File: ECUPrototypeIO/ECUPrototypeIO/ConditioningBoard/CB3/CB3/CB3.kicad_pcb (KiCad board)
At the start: 2 copper layers, 28 parts, among them J1 ECU Connector 1, J2 ECU Connector 2, J3 Relay Module Con2, J4 Vehicle Connector 1, J5 Relay Module Con1, Q1 MOSFET_A, SW1 MomentarySwitch, SW2 MomentarySwitch, T1 Screw_Terminal_01x04, U1 LM324

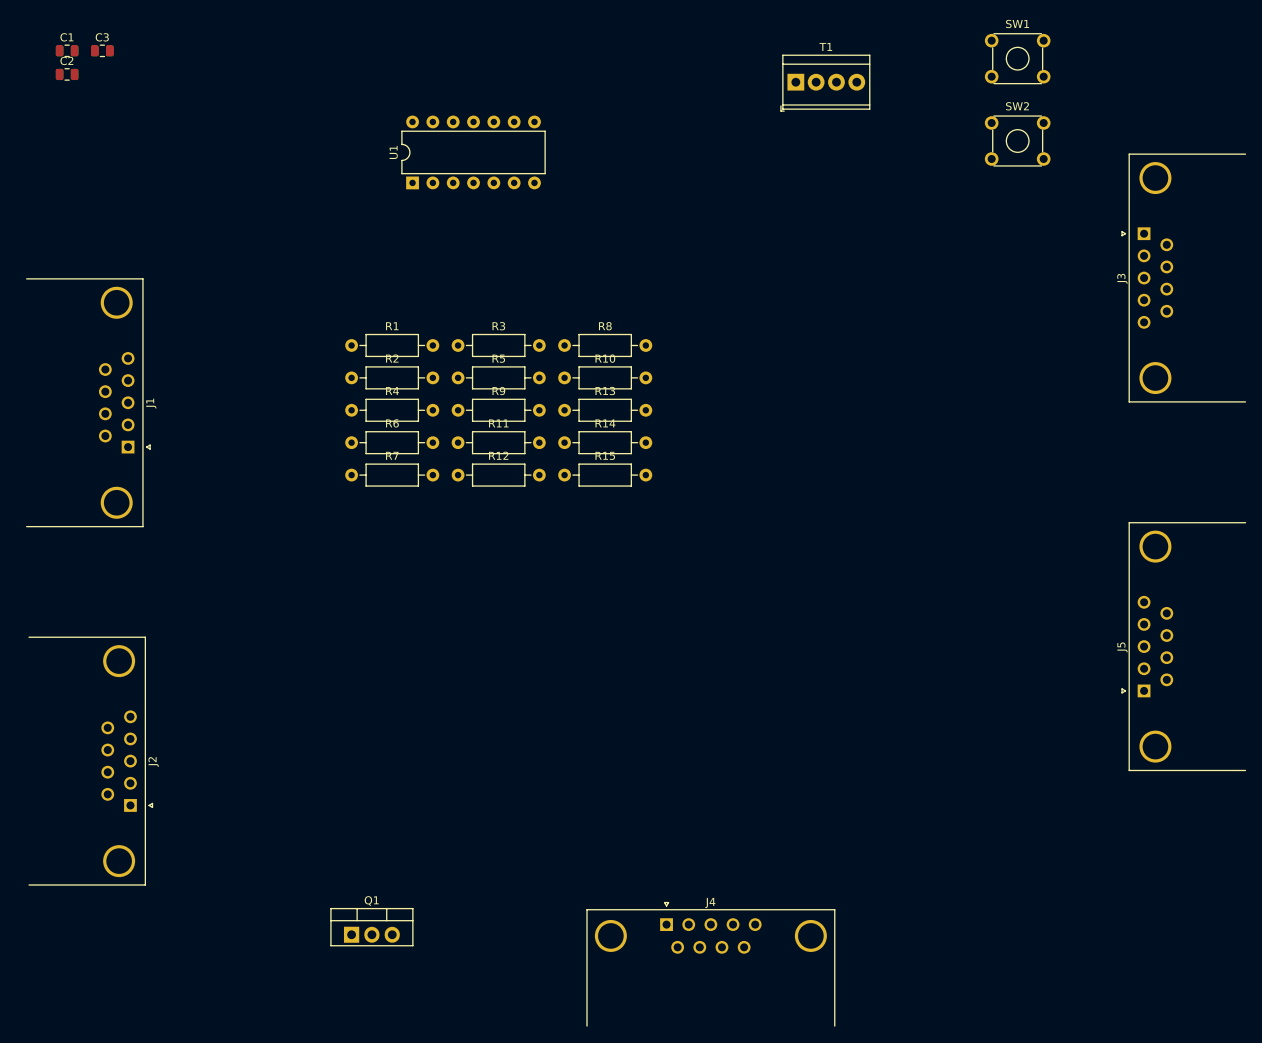
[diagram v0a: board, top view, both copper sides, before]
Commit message: grouped relevant components on PCB Schematic
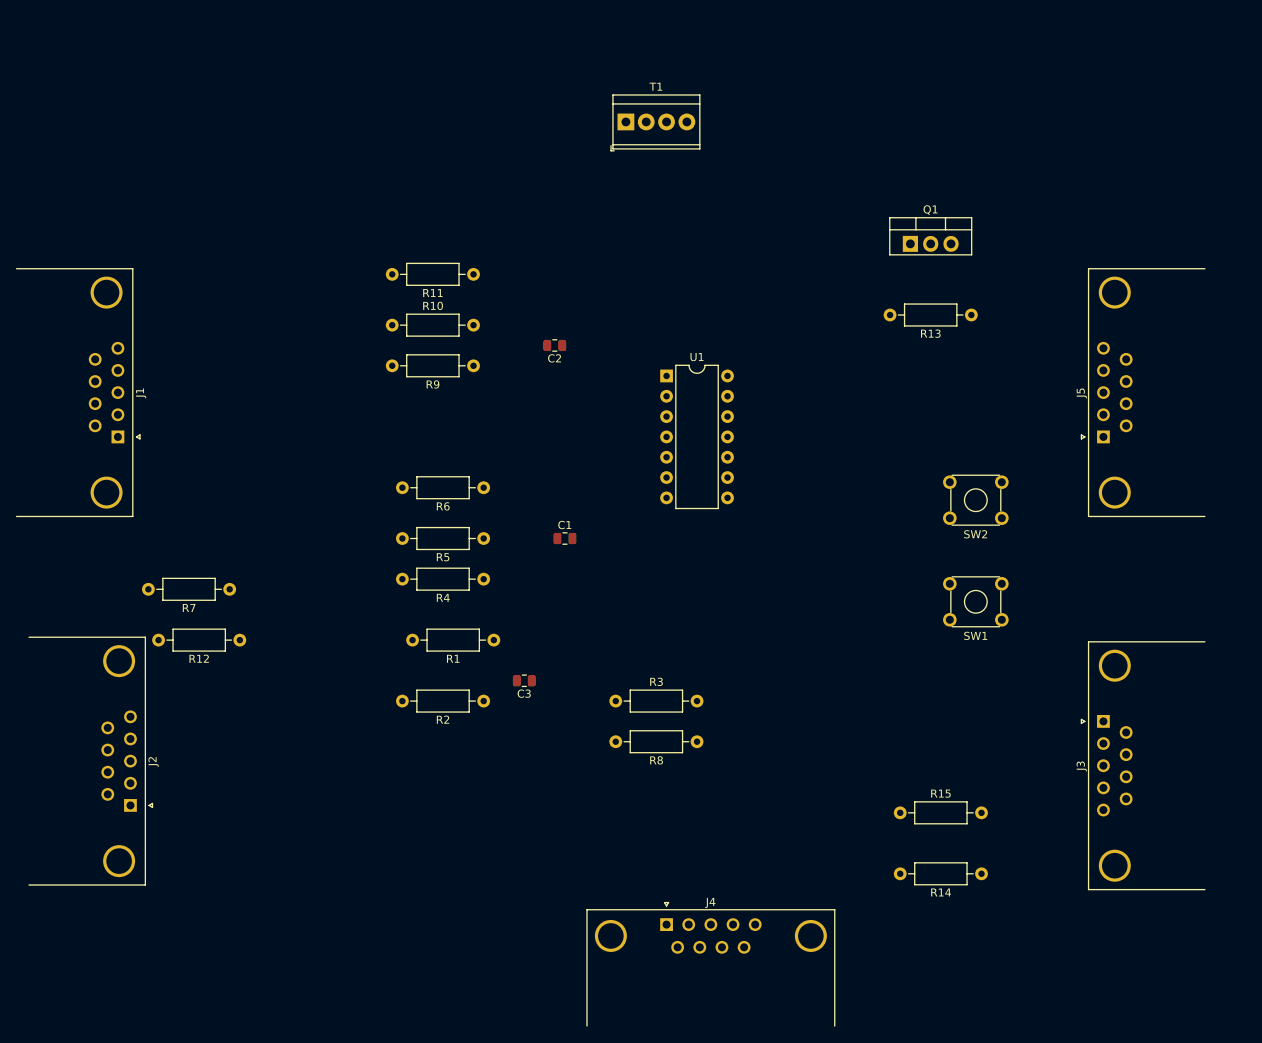
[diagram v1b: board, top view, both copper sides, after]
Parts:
- moved Q1 111.1 mm to (167.6, 44.5)
- moved C3 94.8 mm to (119.4, 99.1), turned to 180 degrees
- moved C1 87.1 mm to (124.5, 81.3)
- moved R14 75.0 mm to (176.5, 123.2), turned to 180 degrees
- moved SW1 72.4 mm to (179.1, 91.4), turned to 180 degrees
- moved C2 69.7 mm to (123.2, 57.1), turned to 180 degrees
- moved J3 61.2 mm to (191.8, 104.1)
- moved R15 59.5 mm to (166.4, 115.6)
- moved R13 52.2 mm to (175.3, 53.3), turned to 180 degrees
- moved R8 52.2 mm to (141.0, 106.7), turned to 180 degrees
- moved SW2 49.4 mm to (179.1, 78.7), turned to 180 degrees
- moved R3 48.6 mm to (130.8, 101.6)
- moved R2 43.6 mm to (114.3, 101.6), turned to 180 degrees
- moved R1 40.9 mm to (115.6, 94.0), turned to 180 degrees
- moved U1 39.9 mm to (137.2, 61.0), turned to 0 degrees
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
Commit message: 1st Draft PCB completed; Import dsn file to view complete layout
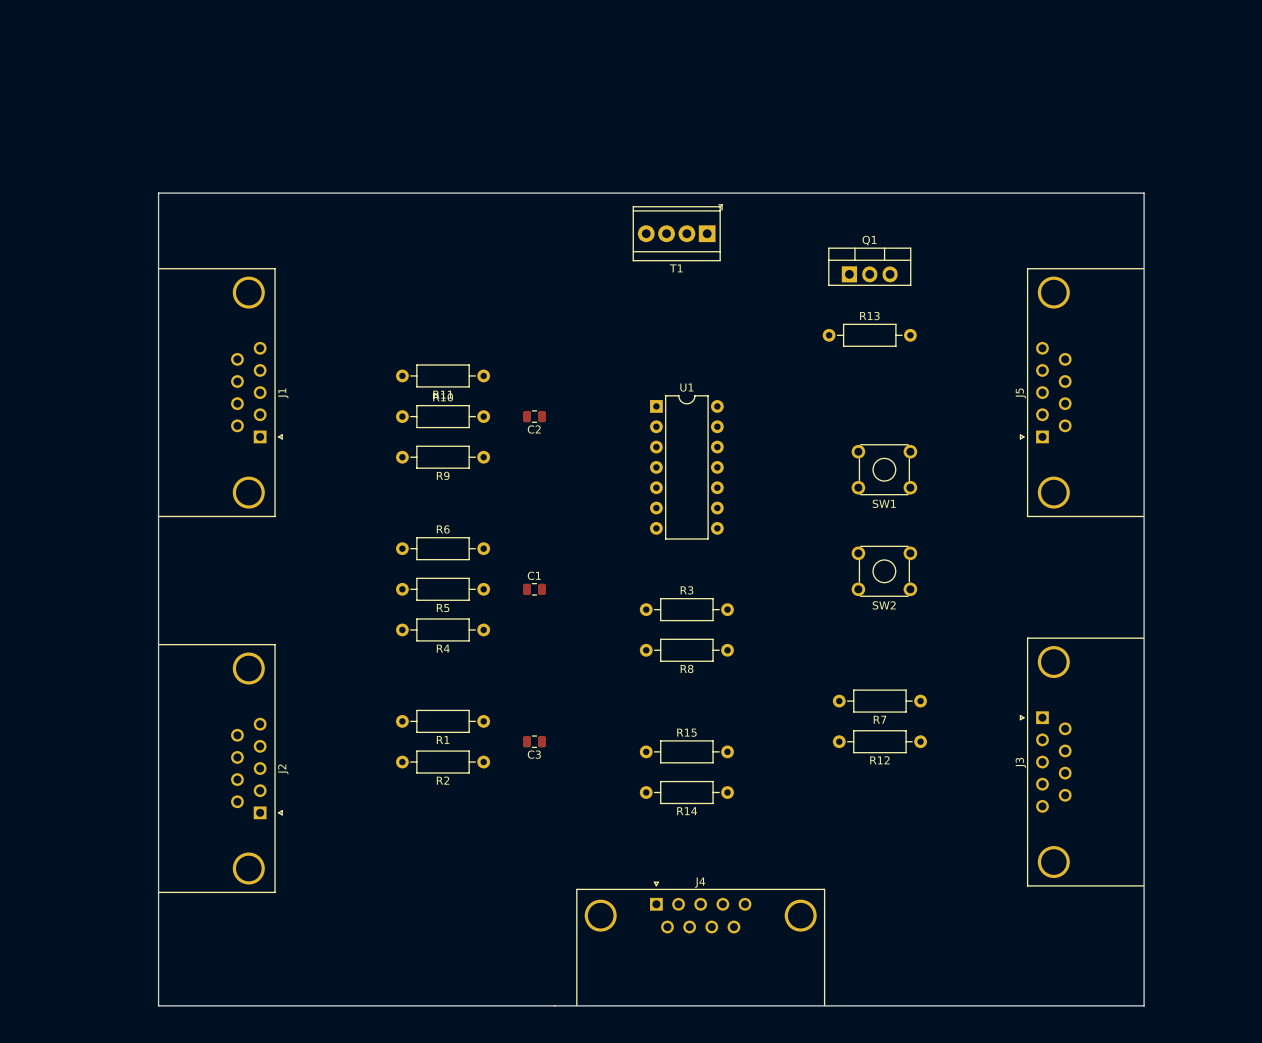
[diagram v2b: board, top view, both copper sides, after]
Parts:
- moved R7 87.5 mm to (168.9, 101.6)
- moved R12 86.0 mm to (168.9, 106.7)
- moved R14 33.3 mm to (144.8, 113.0)
- moved R15 32.7 mm to (134.6, 108.0)
- moved SW1 20.1 mm to (167.6, 74.9)
- moved R13 18.0 mm to (157.5, 55.9), turned to 0 degrees
- moved J1 17.8 mm to (86.4, 68.6)
- moved T1 17.3 mm to (142.2, 43.2), turned to 180 degrees
- moved J2 16.2 mm to (86.4, 115.6)
- moved SW2 14.5 mm to (167.6, 87.6)
- moved R11 12.8 mm to (114.3, 61.0)
- moved R6 12.7 mm to (104.1, 82.5), turned to 0 degrees
- moved R8 12.0 mm to (144.8, 95.2)
- moved R3 12.0 mm to (134.6, 90.2)
- moved R10 11.5 mm to (104.1, 66.0)
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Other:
- board outline added: 123.2 x 101.6 mm

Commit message: latest files from jb laptop, unsure what changes exist
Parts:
- added D1: 3.3V, Diode_THT:D_T-1_P5.08mm_Horizontal, F.Cu at (96.0, 84.3)
- added D2: 1N4001, Diode_THT:D_DO-41_SOD81_P10.16mm_Horizontal, F.Cu at (93.3, 101.4)
- added D3: 5.6V, Diode_THT:D_T-1_P5.08mm_Horizontal, F.Cu at (100.1, 46.3)
- added D4: LD271, LED_THT:LED_D5.0mm_IRGrey, F.Cu at (103.4, 41.9)
- added D5: LD271, LED_THT:LED_D5.0mm_IRGrey, F.Cu at (124.7, 41.9)
- added F1: 1A Fuse, Fuse:Fuse_0805_2012Metric, F.Cu at (104.9, 47.1)
- added R16: 330, Resistor_THT:R_Axial_DIN0207_L6.3mm_D2.5mm_P10.16mm_Horizontal, F.Cu at (100.3, 41.9)
- added R17: 1K, Resistor_THT:R_Axial_DIN0207_L6.3mm_D2.5mm_P10.16mm_Horizontal, F.Cu at (128.0, 41.9)
- C3: moved to B.Cu
- Q1: value MOSFET_A -> 2N7002H; footprint Package_TO_SOT_THT:TO-220-3_Vertical -> Package_TO_SOT_SMD:SOT-23
- R12, R8: value 10K -> 220K
- R3, R7: value 20K -> 330K
- moved J3 60.6 mm to (146.3, 56.4)
- moved R12 58.9 mm to (110.7, 97.5), turned to 0 degrees
- moved SW1 49.7 mm to (136.9, 114.0)
- moved J5 48.9 mm to (146.3, 99.6)
- moved R7 48.6 mm to (120.9, 94.2)
- moved R3 41.3 mm to (93.5, 94.2)
- moved R8 41.2 mm to (103.6, 97.5)
- moved J4 40.8 mm to (101.1, 105.7)
- moved R13 37.7 mm to (120.4, 49.0), turned to 180 degrees
- moved SW2 35.3 mm to (136.9, 104.9)
- moved Q1 34.1 mm to (126.0, 49.3), turned to 270 degrees
- moved R15 26.1 mm to (127.5, 82.8)
- moved R14 26.1 mm to (137.7, 87.9)
- moved U1 24.6 mm to (111.5, 61.5)
- moved T1 24.4 mm to (117.9, 42.4)
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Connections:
- net +12V renamed 12V
- C1 pad 2: ReverseControl_Black -> GND
- C2 pad 2: ReverseControl_Black -> GND
- C3 pad 2: ReverseControl_Black -> GND
- J1 pad 0: (no net) -> GND
- J1 pad 3: ReverseControl_Black -> GND
- J1 pad 9: +5V -> 5V_Fused
- J2 pad 0: (no net) -> GND
- J3 pad 0: (no net) -> GND
- J3 pad 3: ReverseControl_Black -> GND
- J4 pad 0: (no net) -> GND
- J4 pad 2: ReverseControl_Black -> GND
- J4 pad 3: ReverseControl_Black -> GND
- J4 pad 6: ReverseControl_Black -> GND
- J4 pad 9: +5V -> 5V_Fused
- J5 pad 0: (no net) -> GND
- Q1 pad 2: RelayD_NO -> GND
- Q1 pad 3: ReverseControl_Black -> RelayD_NO
- R1 pad 1: MotorSpeed_Red -> Net-(D2-Pad1)
- R10 pad 2: ReverseControl_Black -> GND
- R13 pad 2: +5V -> 5V_Fused
- R14 pad 2: ReverseControl_Black -> GND
- R2 pad 1: ReverseControl_Black -> GND
- R2 pad 2: MotorSpeed_Red -> Net-(D2-Pad1)
- R3 pad 2: ReverseControl_Black -> GND
- R6 pad 2: ReverseControl_Black -> GND
- R7 pad 2: ReverseControl_Black -> GND
- SW1 pad 2: ReverseControl_Black -> GND
- SW2 pad 2: ReverseControl_Black -> GND
- T1 pad 1: ReverseControl_Black -> GND
- T1 pad 3: ReverseControl_Black -> GND
- T1 pad 4: +5V -> 5V
- U1 pad 1: (no net) -> RelayC_NO
- U1 pad 10: Net-(C2-Pad1) -> (no net)
- U1 pad 11: ReverseControl_Black -> GND
- U1 pad 2: (no net) -> Net-(R10-Pad1)
- U1 pad 3: (no net) -> Net-(C2-Pad1)
- U1 pad 8: RelayC_NO -> (no net)
- U1 pad 9: Net-(R10-Pad1) -> (no net)
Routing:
- net 5V_Fused: track 0.00 -> 141.8 mm
- net SteeringDirection: track 0.00 -> 112.2 mm
- net SteeringEnable: track 0.00 -> 111.9 mm
- net 12V: track 0.00 -> 111.3 mm
- net ReverseControl_Blue: track 0.00 -> 88.0 mm
- net Brake: track 0.00 -> 85.3 mm, vias 0 -> 1
- net SafetyLights2Enable: track 0.00 -> 85.3 mm
- net ReverseControl_Red: track 0.00 -> 81.9 mm, vias 0 -> 1
- net SafetyLights1Enable: track 0.00 -> 81.7 mm
- net ESTOP: track 0.00 -> 81.3 mm
- net RelayC_NO: track 0.00 -> 74.1 mm, vias 0 -> 1
- net RelayD_NO: track 0.00 -> 62.0 mm, vias 0 -> 1
- net SteeringDriverConnector1_Yellow: track 0.00 -> 51.3 mm, vias 0 -> 1
- net AccelerationEnable: track 0.00 -> 47.7 mm
- net SteeringEncoderB: track 0.00 -> 40.2 mm, vias 0 -> 1
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- added copper zone on B.Cu, net GND
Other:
- board size 123.2 x 101.6 mm -> 85.3 x 80 mm
- board text added: "10K"
- board text added: "1K"
- board text added: "1M"
- board text added: "220K"
- board text added: "3.3V"
- board text added: "330"
- board text added: "330K"
- board text added: "39K"
- board text added: "5.6K"
- board text added: "5.6V"
- board text added: "8.2K"
- board text added: "EC1"
- board text added: "EC2"
- board text added: "Magic Smoke Goes Here"
- board text added: "Oakland University"
- board text added: "R1"
- board text added: "R2"
- board text added: "SD"
- board text added: "Smart Vehicle Club"

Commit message: Look at README File
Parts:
- C1, C2: footprint Capacitor_SMD:C_0805_2012Metric -> Capacitor_THT:C_Disc_D7.5mm_W5.0mm_P7.50mm
- C3: footprint Capacitor_SMD:C_0805_2012Metric -> Capacitor_THT:C_Disc_D7.5mm_W5.0mm_P7.50mm; moved to F.Cu
- F1: footprint Fuse:Fuse_0805_2012Metric -> Fuse:Fuse_Littelfuse-LVR100
- Q1: footprint Package_TO_SOT_SMD:SOT-23 -> Package_TO_SOT_THT:SIPAK-1EP_Horizontal_TabDown
- moved F1 35.5 mm to (127.0, 74.9)
- moved C3 35.4 mm to (130.8, 94.0), turned to 0 degrees
- moved C1 12.4 mm to (116.8, 87.6)
- moved Q1 2.75 mm to (128.3, 50.8)
- moved C2 2.01 mm to (106.7, 54.6)
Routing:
- net 5V_Fused: track 141.8 -> 187.6 mm, vias 0 -> 1
- net 5V: track 8.56 -> 47.9 mm, vias 0 -> 1
- net MotorSpeed_Red: track 9.83 -> 35.8 mm, vias 0 -> 2
- net Net-(C1-Pad1): track 19.1 -> 35.1 mm
- net AccelerationEnable: track 47.7 -> 50.7 mm
- net Net-(C2-Pad1): track 15.0 -> 17.7 mm
- net ReverseControl_Red: track 81.9 -> 79.7 mm
- net 12V: track 111.3 -> 109.2 mm
- net GND: track 6.59 -> 4.93 mm, vias 3 -> 1
- net SafetyLights1Enable: track 81.7 -> 83.0 mm
- net ReverseControl_Blue: track 88.0 -> 87.1 mm
- net SteeringDriverConnector1_Yellow: track 51.3 -> 51.8 mm
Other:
- board text added: "(Magic Smoke Goes Here)"
- board text added: "Oakland University Smart Vehicle Club"
- board text removed: "Magic Smoke Goes Here"
- board text removed: "Oakland University"
- board text removed: "Smart Vehicle Club"

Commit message: Look at README
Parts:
- added R18: 10k, Resistor_THT:R_Axial_DIN0207_L6.3mm_D2.5mm_P10.16mm_Horizontal, F.Cu at (104.1, 66.0)
- moved R15 6.26 mm to (130.8, 88.1)
- moved R14 5.36 mm to (137.2, 82.5)
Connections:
- R14 pad 1: ESTOP -> VoltageDivider_C
- R14 pad 2: GND -> ESTOP
- R15 pad 1: VoltageDivider_C -> GND
- R15 pad 2: ESTOP -> VoltageDivider_C
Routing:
- net AccelerationEnable: track 50.7 -> 89.6 mm
- net ESTOP: track 81.3 -> 61.8 mm
- net VoltageDivider_C: track 32.0 -> 22.5 mm
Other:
- board text removed: "39K"
